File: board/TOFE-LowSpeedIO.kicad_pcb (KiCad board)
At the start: 2 copper layers, 1 part

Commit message: Creating TOFE-LowSpeedIO!
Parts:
- removed the U? at (148.4, 164.6)
- added U?: TOFE_LowSpeedIO_Expansion_Board_8x_FullHeight, TOFE_8X_FullHeight, F.Cu at (125.1, 196.7)

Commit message: Initial drop of TOFE LowSpeedIO Expansion Board.
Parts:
- removed U?: TOFE_LowSpeedIO_Expansion_Board_8x_FullHeight, TOFE_8X_FullHeight
- added 1PIN: P***, MH-3.2MM, F.Cu at (232.0, 84.0)
- added 1PIN: P***, MH-3.2MM, F.Cu at (232.0, 172.0)
- added C1: 22pF, SM0603, F.Cu at (163.1, 164.1)
- added C10: 0.1uF, SM0603, F.Cu at (214.4, 98.3)
- added C2: 22pF, SM0603, F.Cu at (163.1, 169.2)
- added C3: 0.1uF, SM0603, F.Cu at (142.5, 169.4)
- added C4: 0.1uF, SM0603, F.Cu at (153.9, 172.0)
- added C8: 100uF, SM1210L, F.Cu at (206.0, 99.1)
- added C9: 100uF, SM1210L, F.Cu at (211.1, 99.1)
- added D1: LED, LED-0805-New, F.Cu at (171.7, 85.9)
- added D2: LED, LED-0805-New, F.Cu at (174.8, 85.9)
- added D3: LED, LED-0805-New, F.Cu at (177.8, 85.9)
- added D4: DIODE, DO214, F.Cu at (183.6, 99.1)
- added D5: LED, LED-0805-New, F.Cu at (168.7, 85.9)
- added D6: LED, LED-0805-New, F.Cu at (165.6, 85.9)
- added D7: LED, LED-0805-New, F.Cu at (180.8, 85.9)
- added G***: LOGO, LOGO_BOTTOM, F.Cu at (184.2, 171.4)
- added P1: CONN_6X2, pin_array_6x2, F.Cu at (140.2, 129.8)
- added P2: CONN_6X2, pin_array_6x2, F.Cu at (140.2, 109.5)
- added P3: CONN_6X2, pin_array_6x2, F.Cu at (153.9, 90.2)
- added P4: CONN_6X2, pin_array_6x2, F.Cu at (140.2, 150.4)
- added P5: CONN_2, PIN_ARRAY_2X1, F.Cu at (166.9, 174.5)
- added P6: CONN_6, PIN_ARRAY-6X1, F.Cu at (151.4, 174.5)
- added R1: 10K, SM0603, F.Cu at (166.4, 171.2)
- added R10: 100R, SM0603, F.Cu at (143.0, 162.8)
- added R2: 10K, SM0603, F.Cu at (153.7, 160.0)
- added R3: 10K, SM0603, F.Cu at (200.9, 157.5)
- added R4: 680R, RES_NET4, F.Cu at (184.4, 94.0)
- added R5: 10K, RES_NET4, F.Cu at (170.4, 94.0)
- added R6: 10K, SM0603, F.Cu at (193.8, 100.8)
- added R7: 10K, SM0603, F.Cu at (150.6, 160.0)
- added R8: 10K, SM0603, F.Cu at (145.8, 161.0)
- added R9: 10K, SM0603, F.Cu at (142.2, 166.1)
- added SW1: SW_PUSH, Switch_SMD, F.Cu at (187.5, 85.3)
- added SW2: SW_PUSH, Switch_SMD, F.Cu at (192.0, 85.3)
- added SW3: SW_PUSH, Switch_SMD, F.Cu at (196.6, 85.3)
- added SW4: SW_PUSH, Switch_SMD, F.Cu at (201.2, 85.3)
- added U1: TIMVIDEOS-PCIE-8X, NumatoOpsis_PCIe_8X_HL_NW, F.Cu at (129.0, 185.7)
- added U2: AURD_COMM_SHIELD_ZERO_NEW, ARDUINO-UNO-R3_1_NEW, F.Cu at (191.3, 129.0)
- added U3: PIC18F14K50, SSOP-20, F.Cu at (149.4, 167.4)
- added U5: 7805_NW, DPAK2, F.Cu at (208.8, 92.1)
- added X1: CRYSTAL, HC-49V, F.Cu at (158.2, 166.6)
- added X2: USBMICRO, MICRO_USB_B, F.Cu at (130.6, 166.9)
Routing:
- net /VCC3V3: track 0.00 -> 365.5 mm, vias 0 -> 15
- net /GND: track 0.00 -> 259.1 mm, vias 0 -> 87
- net /VCC12V: track 0.00 -> 244.6 mm, vias 0 -> 4
- net /RESET: track 0.00 -> 176.5 mm, vias 0 -> 4
- net /GPIO5_P: track 0.00 -> 169.8 mm
- net /D8: track 0.00 -> 135.1 mm, vias 0 -> 1
- net /D10: track 0.00 -> 133.4 mm
- net /D14: track 0.00 -> 133.1 mm
- net /D12: track 0.00 -> 133.0 mm
- net /D11: track 0.00 -> 132.4 mm, vias 0 -> 1
- net /D15: track 0.00 -> 130.4 mm
- net /D13: track 0.00 -> 130.2 mm, vias 0 -> 1
- net /D9: track 0.00 -> 129.7 mm
- net /GPIO7_N: track 0.00 -> 128.5 mm
- net /LED3: track 0.00 -> 127.7 mm
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- added copper zone on B.Cu, net /GND
- added copper zone on F.Cu, net /GND
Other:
- board outline added: 108 x 111.2 mm
- net class Default: clearance 0.254 -> 0.2032
- rule trace_clearance: 0.254 -> 0.2032
- rule trace_min: 0.254 -> 0.127
- rule via_min_drill: 0.508 -> 0.254
- rule via_min_size: 0.889 -> 0.4572
- board text added: "1"
- board text added: "11"
- board text added: "12"
- board text added: "2"
- board text added: "3V3"
- board text added: "Arduino Shield Compatible (3V3)"
- board text added: "FWUP"
- board text added: "GND"
- board text added: "ICSP"
- board text added: "LED1"
- board text added: "LED2"
- board text added: "LED3"
- board text added: "LED4"
- board text added: "LED5"
- board text added: "LED6"
- board text added: "NUMATO LAB TOFE Low Speed IO Expansion Board www.numato.com"
- board text added: "Rev1"

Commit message: Changes on 2015-11-03.
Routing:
- net /LED2: track 115.1 -> 117.2 mm
- net /LED1: track 116.5 -> 118.6 mm
- net /LED4: track 113.2 -> 115.1 mm
- net N-0000054: track 115.3 -> 113.6 mm
- net N-0000055: track 110.6 -> 109.7 mm
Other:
- net class Default: via_dia 0.889 -> 0.4572; via_drill 0.635 -> 0.254
- board text added: "NUMATO LAB Opsis TOFE Low Speed IO Module www.numato.com"
- board text removed: "NUMATO LAB TOFE Low Speed IO Expansion Board www.numato.com"

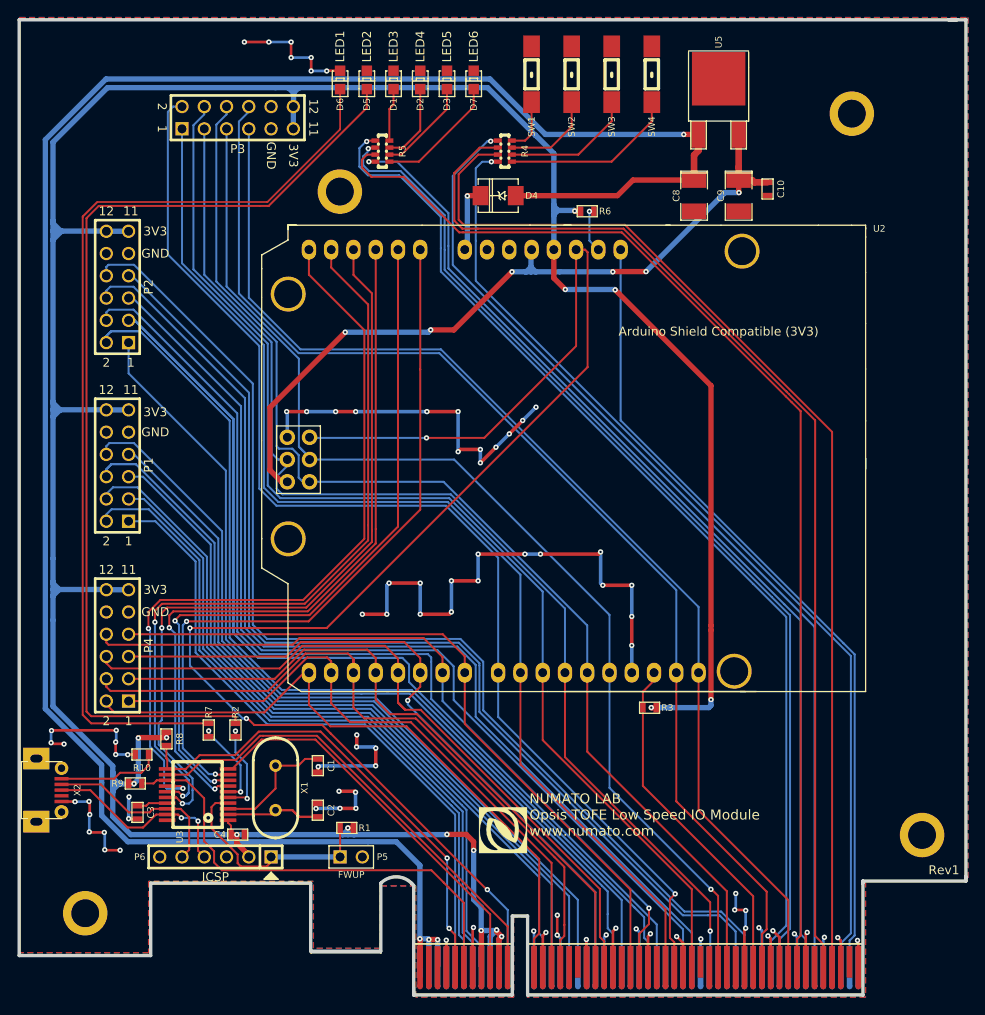
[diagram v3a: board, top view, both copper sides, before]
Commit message: Mounting holes rearrangements.
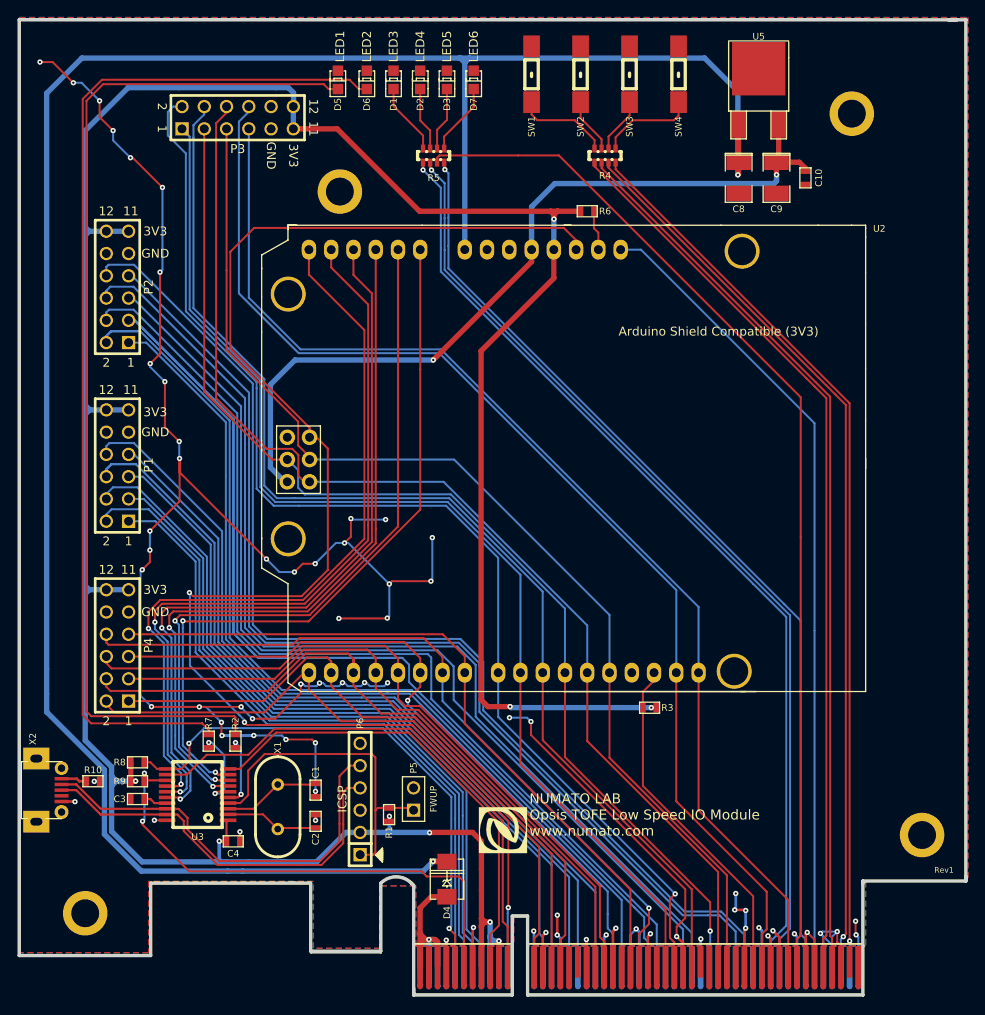
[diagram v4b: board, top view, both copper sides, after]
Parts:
- SW1, SW2, SW3, SW4: footprint Switch_SMD -> Switch_SMD_new
- moved D4 78.2 mm to (177.8, 177.0), turned to 90 degrees
- moved P6 17.8 mm to (167.9, 167.9), turned to 90 degrees
- moved R4 11.4 mm to (195.8, 94.5), turned to 180 degrees
- moved P5 9.71 mm to (174.0, 167.9), turned to 90 degrees
- moved R10 6.37 mm to (137.4, 165.9), turned to 0 degrees
- moved R5 5.86 mm to (176.3, 94.5), turned to 180 degrees
- moved C8 5.47 mm to (211.1, 97.0)
- moved R1 5.06 mm to (171.2, 169.7), turned to 90 degrees
- moved C9 4.77 mm to (215.4, 97.0)
- moved U5 4.71 mm to (213.4, 90.9)
- moved C10 4.50 mm to (218.7, 97.0)
- moved R8 4.24 mm to (142.5, 163.7), turned to 180 degrees
- moved D5 3.30 mm to (165.4, 85.9)
- moved D6 3.05 mm to (168.7, 85.9)
- moved SW4 3.05 mm to (204.2, 85.3)
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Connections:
- D4 pad 1: /VCC12V -> /12V
- D4 pad 2: /12V -> /VCC12V
- U1 pad A2: /VCC12V -> /12V
- U1 pad A3: /VCC12V -> /12V
- U1 pad A44: /SW1 -> /ATN
- U1 pad A47: /SW4 -> /SW3
- U1 pad A48: /ATN -> /SW4
- U1 pad B1: /VCC12V -> /12V
- U1 pad B2: /VCC12V -> /12V
- U1 pad B3: /VCC12V -> /12V
- U1 pad B33: /D13 -> /D12
- U1 pad B34: /D12 -> /D13
- U1 pad B45: /SW2 -> /SW1
- U1 pad B46: /SW3 -> /SW2
- U2 pad : (no net) -> /GND
- U2 pad 8: /12V -> /VCC12V
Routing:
- net /GND: track 259.1 -> 363.2 mm, vias 87 -> 73
- net /PGC: track 22.7 -> 47.4 mm
- net /PGD: track 22.6 -> 45.3 mm, vias 2 -> 0
- net /SW2: track 124.9 -> 102.6 mm
- net /SW3: track 124.2 -> 103.7 mm, vias 0 -> 1
- net /12V: track 7.77 -> 28.1 mm
- net /VCC3V3: track 365.5 -> 347.2 mm, vias 15 -> 9
- net /VPP: track 25.7 -> 38.2 mm
- net /SW1: track 114.1 -> 102.8 mm, vias 1 -> 0
- net N-0000055: track 109.7 -> 119.6 mm
- net /SW4: track 112.1 -> 102.8 mm
- net /LED3: track 127.7 -> 118.7 mm
- net N-0000038: track 20.1 -> 11.0 mm
- net /LED1: track 118.6 -> 109.6 mm
- net N-0000052: track 11.8 -> 2.94 mm
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
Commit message: Small update to board layout.
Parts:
- removed the 1PIN at (232.0, 84.0)
- added 1PIN: P***, 1pin, F.Cu at (92.5, 50.2)
- U1: footprint NumatoOpsis_PCIe_8X_HL_NW -> NumatoOpsis_PCIe_8X_HL_NW_123
- moved C8 56.6 mm to (169.2, 58.9)
- moved D4 56.6 mm to (135.9, 138.9)
- moved D3 56.6 mm to (135.9, 47.8)
- moved D7 56.6 mm to (138.9, 47.8)
- moved U5 56.6 mm to (171.4, 52.8)
- moved D5 56.6 mm to (123.4, 47.8)
- moved D6 56.6 mm to (126.7, 47.8)
- moved P3 56.6 mm to (112.0, 52.1)
- moved P6 56.6 mm to (126.0, 129.8)
- moved R7 56.6 mm to (108.7, 123.2)
- moved U3 56.6 mm to (107.4, 129.3)
- moved X1 56.6 mm to (116.6, 130.7)
- moved X2 56.6 mm to (88.6, 128.8)
- moved C10 56.6 mm to (176.8, 58.9)
- moved C9 56.6 mm to (173.5, 58.9)
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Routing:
- net /GND: track 363.2 -> 676.7 mm, vias 73 -> 105
- net /VCC3V3: track 347.2 -> 367.4 mm
- net /12V: track 28.1 -> 46.6 mm
- net /RESET: track 169.6 -> 179.9 mm
- net /GPIO6_N: track 121.0 -> 130.9 mm
- net /D7: track 82.6 -> 91.0 mm
- net /GPIO3_N: track 92.7 -> 100.4 mm
- net /GPIO4_N: track 112.8 -> 120.4 mm
- net /D1: track 76.4 -> 81.7 mm
- net /TX: track 53.7 -> 58.9 mm
- net /GPIO6_P: track 114.5 -> 119.6 mm
- net /D10: track 133.7 -> 138.8 mm
- net /GPIO0_N: track 80.6 -> 85.7 mm
- net /SDA: track 58.6 -> 63.6 mm
- net /RX: track 61.6 -> 66.4 mm
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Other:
- rule via_min_size: 0.4572 -> 0.127
- board text added: "NUMATO LAB TOFE Low Speed IO Module www.numato.com"
- board text added: "Rev2.0"
- board text removed: "NUMATO LAB Opsis TOFE Low Speed IO Module www.numato.com"
- board text removed: "Rev1"

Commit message: Trying to fix the Pmod connector labeling.
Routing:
- net /GPIO2_P: track 86.9 -> 42.0 mm
- net /GND: track 676.7 -> 697.7 mm
- net /GPIO0_N: track 85.7 -> 93.3 mm
- net /GPIO3_N: track 100.4 -> 107.9 mm
- net /GPIO3_P: track 89.7 -> 95.9 mm
- net /GPIO1_N: track 85.4 -> 88.9 mm
- net /GPIO2_N: track 95.1 -> 92.6 mm
- net /GPIO1_P: track 80.7 -> 82.3 mm
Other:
- board text added: "6"
- board text added: "7"
- board text removed: "11"
- board text removed: "2"

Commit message: Fixing the PCB.
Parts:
- P1, P2, P3, P4: value CONN_6X2 -> PMOD-CONN_6X2; footprint pin_array_6x2 -> PMOD:pmod_pin_array_6x2
- U1: value TIMVIDEOS-PCIE-8X -> TOFE-8X
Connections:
- P1 pad 10: /GND -> /GPIO3_N
- P1 pad 11: /VCC3V3 -> /GND
- P1 pad 2: /GPIO0_N -> /GPIO1_P
- P1 pad 3: /GPIO1_P -> /GPIO2_P
- P1 pad 4: /GPIO1_N -> /GPIO3_P
- P1 pad 5: /GPIO2_P -> /GND
- P1 pad 6: /GPIO2_N -> /VCC3V3
- P1 pad 7: /GPIO3_P -> /GPIO0_N
- P1 pad 8: /GPIO3_N -> /GPIO1_N
- P1 pad 9: /GND -> /GPIO2_N
- P2 pad 10: /GND -> /GPIO7_N
- P2 pad 11: /VCC3V3 -> /GND
- P2 pad 2: /GPIO4_N -> /GPIO5_P
- P2 pad 3: /GPIO5_P -> /GPIO6_P
- P2 pad 4: /GPIO5_N -> /GPIO7_P
- P2 pad 5: /GPIO6_P -> /GND
- P2 pad 6: /GPIO6_N -> /VCC3V3
- P2 pad 7: /GPIO7_P -> /GPIO4_N
- P2 pad 8: /GPIO7_N -> /GPIO5_N
- P2 pad 9: /GND -> /GPIO6_N
- P3 pad 10: /GND -> /D14
- P3 pad 11: /VCC3V3 -> /GND
- P3 pad 2: /D8 -> /D11
- P3 pad 3: /D11 -> /D13
- P3 pad 4: /D10 -> /D15
- P3 pad 5: /D13 -> /GND
- P3 pad 6: /D12 -> /VCC3V3
- P3 pad 7: /D15 -> /D8
- P3 pad 8: /D14 -> /D10
- P3 pad 9: /GND -> /D12
- P4 pad 10: /GND -> /D6
- P4 pad 11: /VCC3V3 -> /GND
- P4 pad 2: /D0 -> /D3
- P4 pad 3: /D3 -> /D5
- P4 pad 4: /D2 -> /D7
- P4 pad 5: /D5 -> /GND
- P4 pad 6: /D4 -> /VCC3V3
- P4 pad 7: /D7 -> /D0
- P4 pad 8: /D6 -> /D2
- P4 pad 9: /GND -> /D4
- P6 pad 6: (no net) -> Net-(P6-Pad6)
- U1 pad : /GND -> (no net)
- U1 pad A1: (no net) -> Net-(U1-PadA1)
- U1 pad A33: (no net) -> Net-(U1-PadA33)
- U1 pad B17: (no net) -> Net-(U1-PadB17)
- U1 pad B31: (no net) -> Net-(U1-PadB31)
- U1 pad B48: (no net) -> Net-(U1-PadB48)
- U2 pad : /GND -> (no net)
- X2 pad : /GND -> (no net)
- X2 pad 4: (no net) -> Net-(X2-Pad4)
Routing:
- net /GPIO2_P: track 42.0 -> 86.9 mm
- net /GND: track 697.7 -> 676.7 mm
- net /GPIO0_N: track 93.3 -> 85.7 mm
- net /GPIO3_N: track 107.9 -> 100.4 mm
- net /GPIO3_P: track 95.9 -> 89.7 mm
- net /GPIO1_N: track 88.9 -> 85.4 mm
- net /GPIO2_N: track 92.6 -> 95.1 mm
- net /GPIO1_P: track 82.3 -> 80.7 mm
